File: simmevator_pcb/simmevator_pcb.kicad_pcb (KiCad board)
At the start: 2 copper layers, 63.1 x 32.5 mm, 6 parts, among them J1 PWR_IN, J2 BUCKREG, J3 BMP390, U1 XIAO-ESP32-S3-SMD

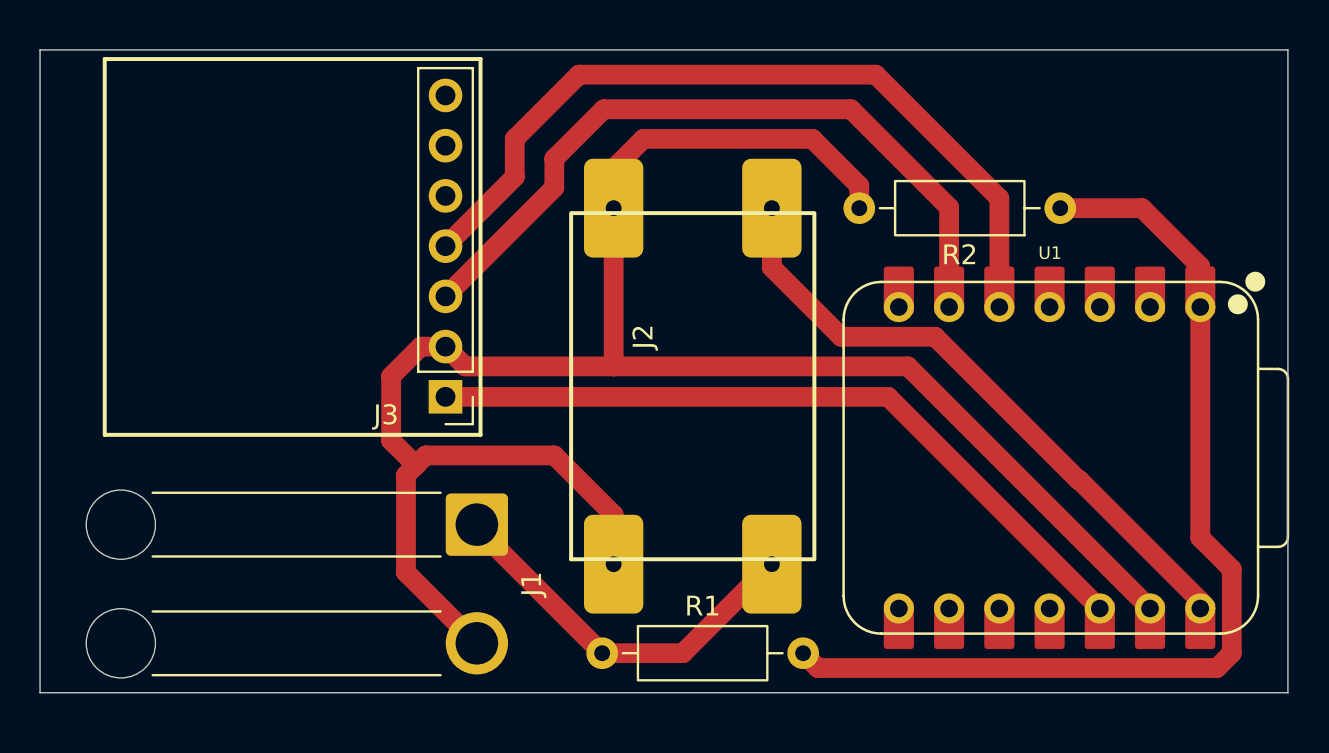
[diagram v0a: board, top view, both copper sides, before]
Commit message: Transmitter PCB: tighten DRC to fab minimums, export gerbers
The DRC constraints were at KiCad's permissive defaults, which let the
router produce geometry no cheap fab will take: 0.2 mm tracks, 0.3 mm
drills, and zero minimum clearance. Raise the floor to what a standard
2-layer process quotes without an upcharge - 0.4 mm clearance, 0.4 mm
track width, 0.4 mm minimum hole and hole clearance - and re-route the
two segments that violated it.

Also commits the fabrication output under fab/: back copper, edge cuts,
the job file and the drill file. They are generated, but they are the
artifact that actually gets ordered, so pinning them to the board
revision that produced them is worth the diff.
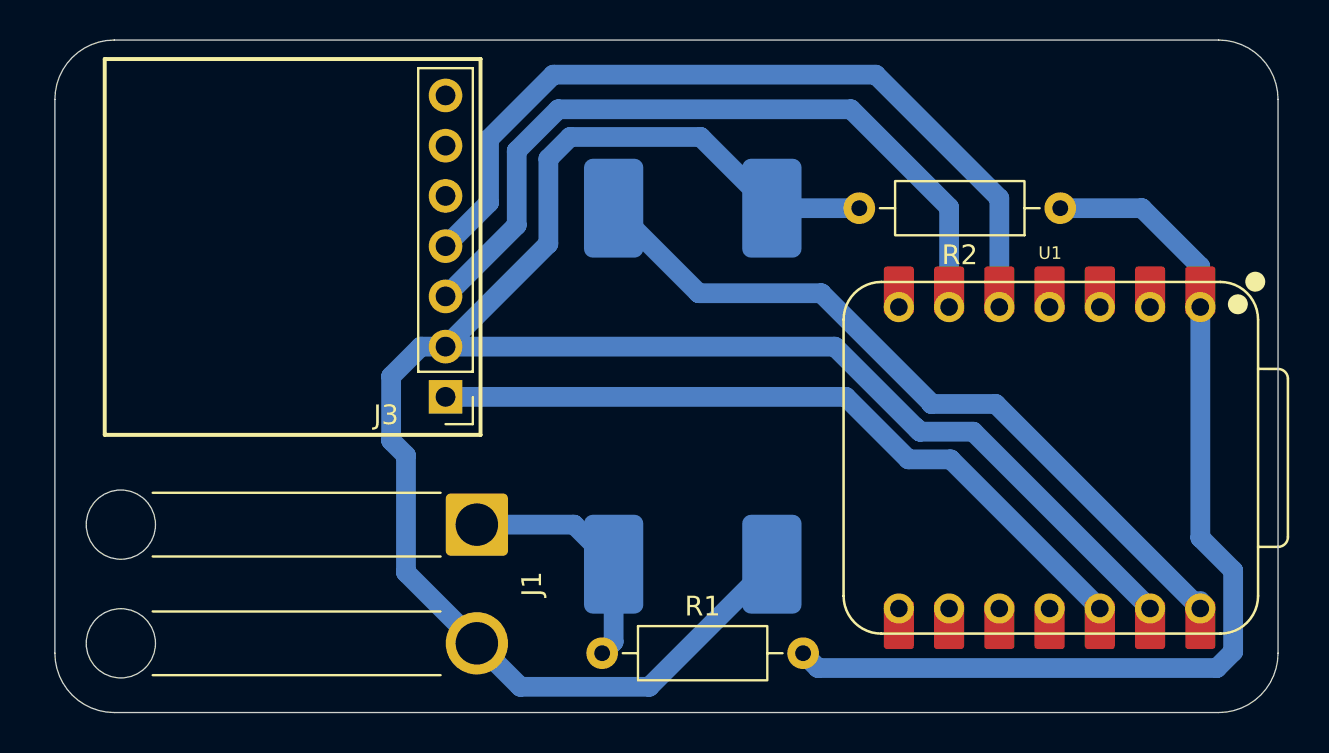
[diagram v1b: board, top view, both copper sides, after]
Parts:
- J2: moved to B.Cu
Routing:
- net GND: track 99.3 -> 106.3 mm
- net +12V: track 19.6 -> 12.6 mm
- net +5V: track 32.9 -> 39.3 mm
- net /SCL: track 36.5 -> 37.8 mm
- net /SDA: track 40.0 -> 40.7 mm
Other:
- board size 63.1 x 32.5 mm -> 61.8 x 34 mm
